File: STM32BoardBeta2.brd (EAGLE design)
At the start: 100 x 63.1 mm, 64 parts, among them IC2 LM2576S, IC3 LM1117IDTX-3.3, IC4 FT232RL, J1 DCJ0202, Q1 8MHz, Q2 32.768KHz, SW1 BOOT, U1 STM32F410R3, X1 MINI-USB-32005-201

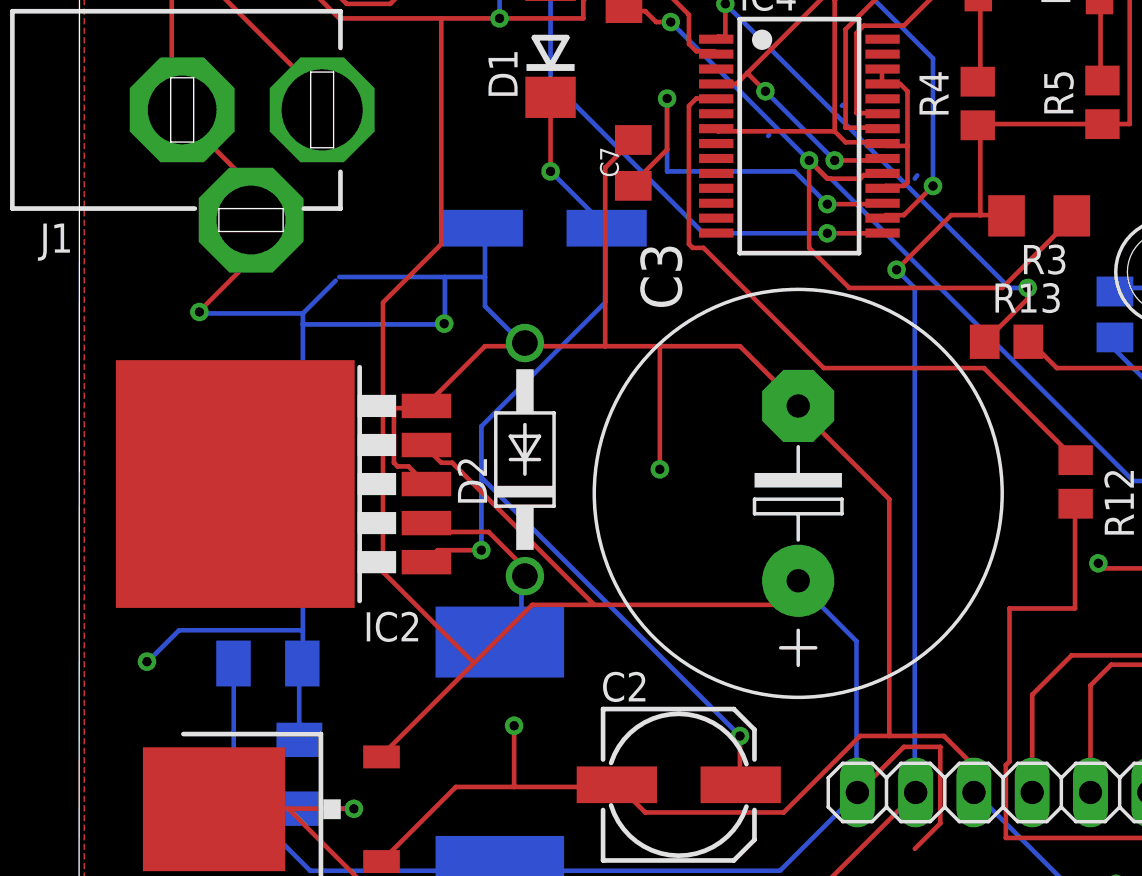
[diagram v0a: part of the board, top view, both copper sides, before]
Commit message: Cambios en condensador y diodo
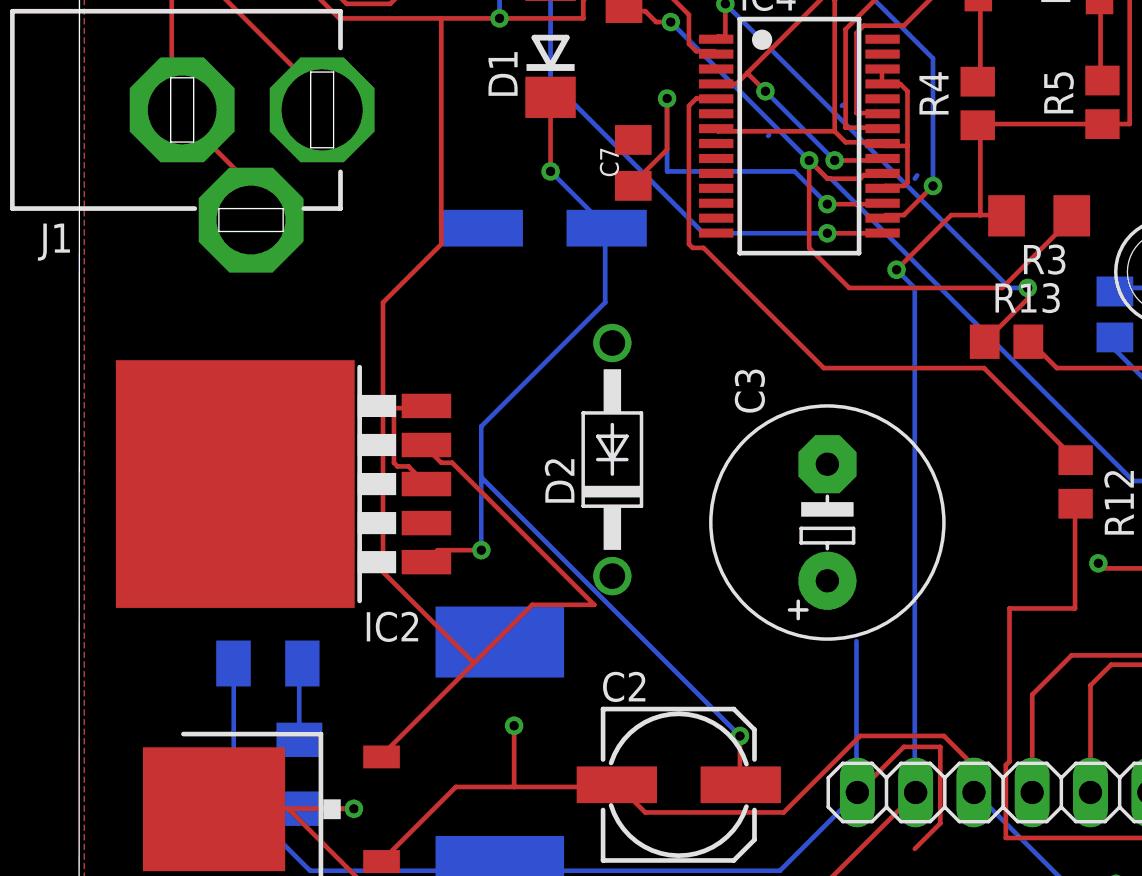
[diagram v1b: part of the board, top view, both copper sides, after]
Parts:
- C3: device rcl:E7,5-18 -> rcl:E5-10,5
- moved D2 3.81 mm to (62.4, 50.0)
- moved C3 1.80 mm to (71.8, 47.2)
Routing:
- net GND: track 703.6 -> 599.2 mm, vias 36 -> 32
- net 5V: track 245.5 -> 232.4 mm
- net N$4: track 8.94 -> 1.27 mm

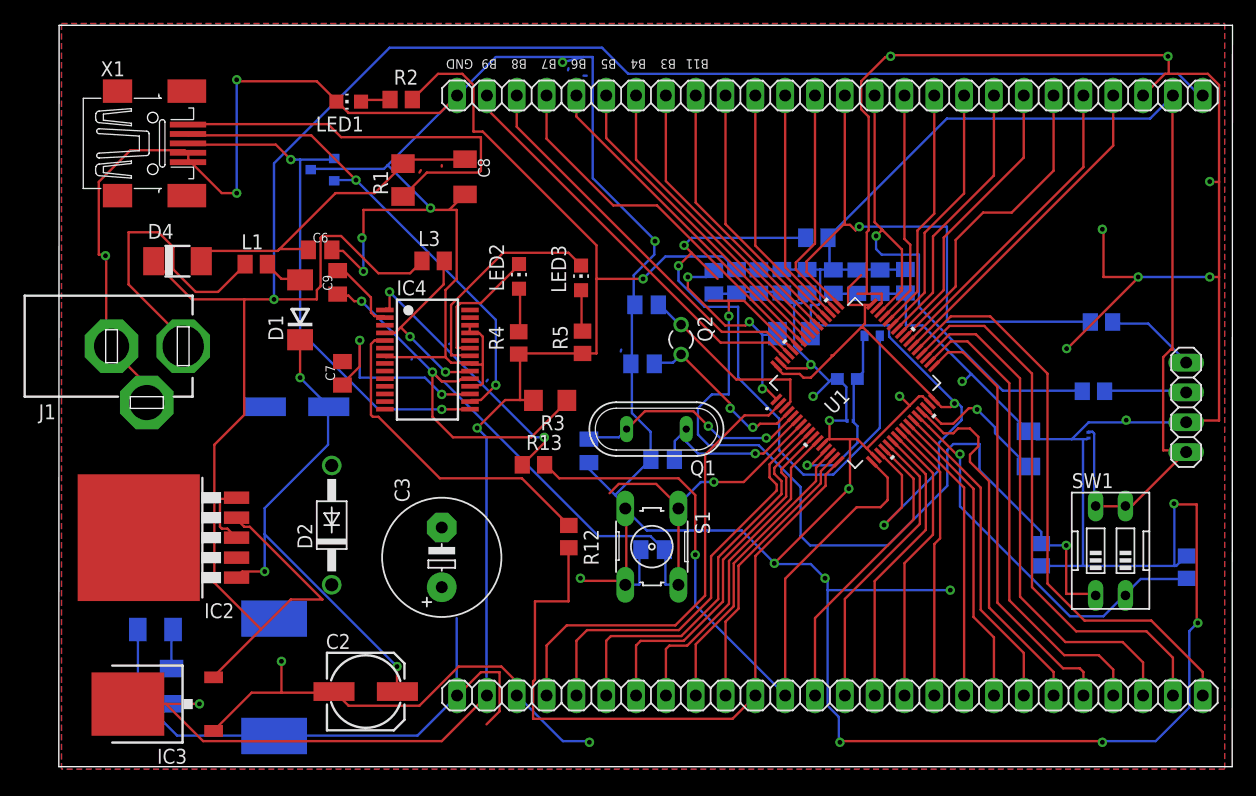
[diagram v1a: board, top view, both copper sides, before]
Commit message: Actualización del diodo 1N5822, SS34 y cambio del tamaño del condensador
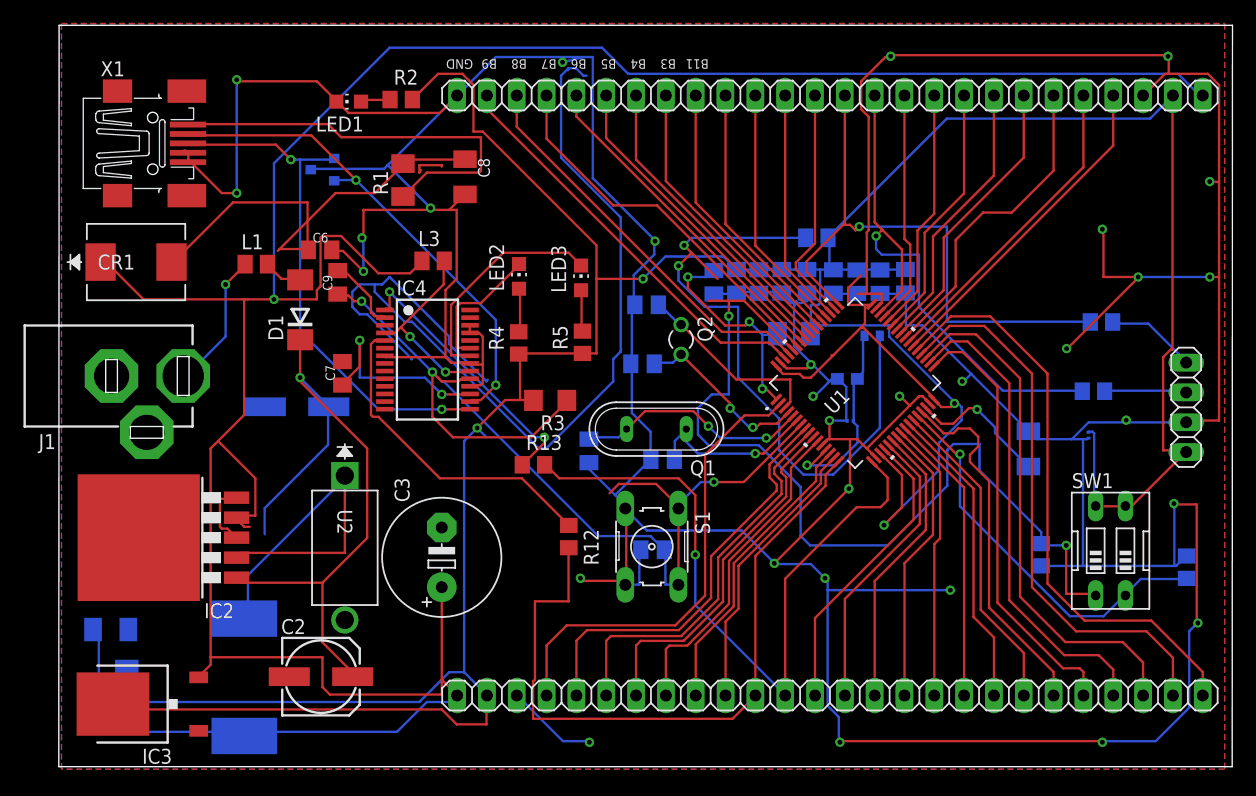
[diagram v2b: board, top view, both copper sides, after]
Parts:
- removed D2: 1N5822, diode:DO41-10
- removed D4: SS34, diode:DO-214AC
- added CR1: SS34, ss34:DIODE_DO214AB-M
- added U2: 1N5822, 1N5822:CASE_267-05
- IC3: value LM1117IDTX-3.3 -> LM1117
- moved C2 4.02 mm to (61.5, 37.1)
- moved C4 3.81 mm to (43.6, 41.1)
- moved C5 3.81 mm to (44.9, 36.3)
- moved J1 2.54 mm to (46.6, 62.7)
- moved L2 2.54 mm to (55.6, 37.0)
- moved IC3 1.27 mm to (46.3, 34.7)
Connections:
- net 5V: now also CR1.1; no longer D4.C
- net GND: now also U2.2; no longer D2.A
- net N$4: now also U2.1; no longer D2.C
- net USB5V: now also CR1.2; no longer D4.A
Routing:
- net N$13: track 0.94 -> 84.8 mm
- net GND: track 599.2 -> 534.2 mm, vias 32 -> 30
- net N$4: track 1.27 -> 31.7 mm
- net 3.3V: track 298.2 -> 326.7 mm, vias 5 -> 4
- net 5V: track 232.4 -> 250.0 mm
- net VIN: track 43.7 -> 57.8 mm, vias 3 -> 1
- net V+: track 25.8 -> 11.8 mm, vias 0 -> 1
- net USB5V: track 28.6 -> 39.4 mm
- net N$14: track 0.37 -> 2.91 mm

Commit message: Cambio en los condensadores 0201 a 0805
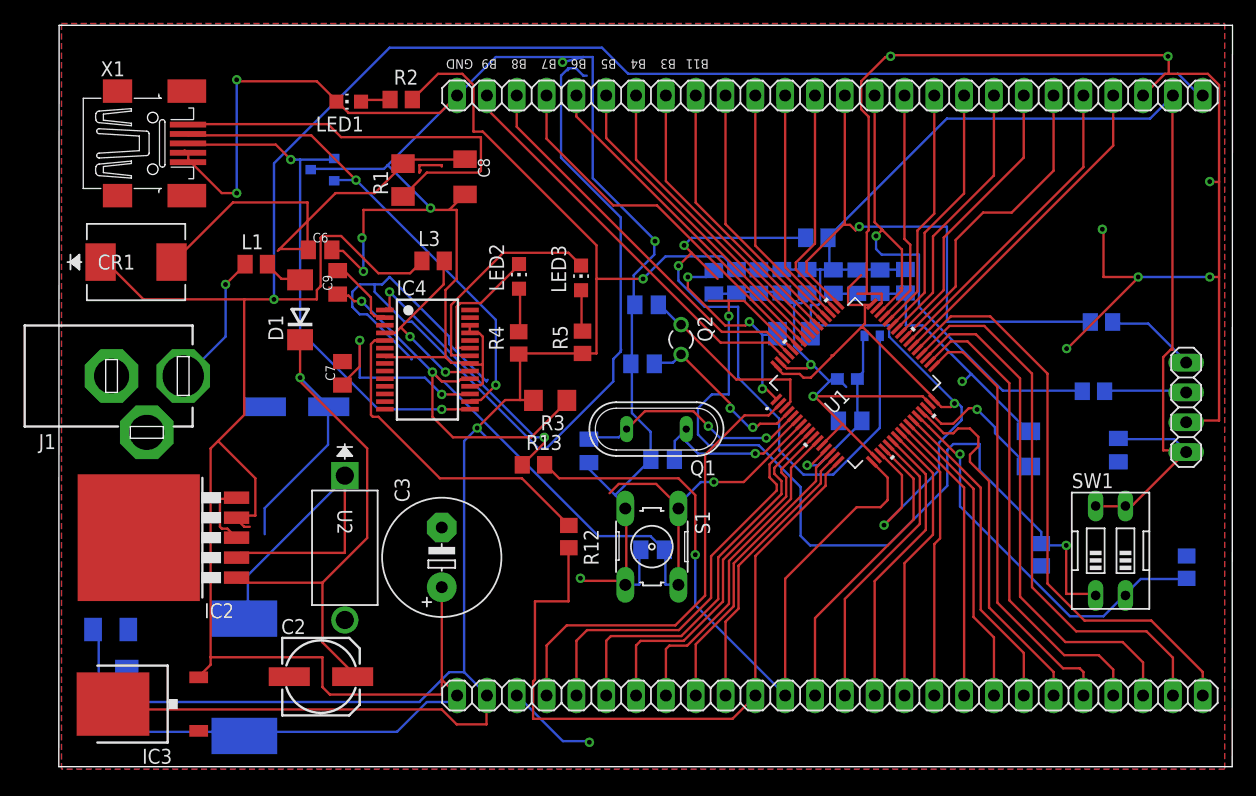
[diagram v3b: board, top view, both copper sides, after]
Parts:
- C11, C29: device rcl:C0201 -> rcl:C0805K
- moved C29 2.84 mm to (129.4, 56.4)
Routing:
- net GND: track 534.2 -> 382.1 mm, vias 30 -> 19
